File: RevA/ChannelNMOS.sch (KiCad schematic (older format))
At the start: 2 parts, among them U2 RAx4_4 1K

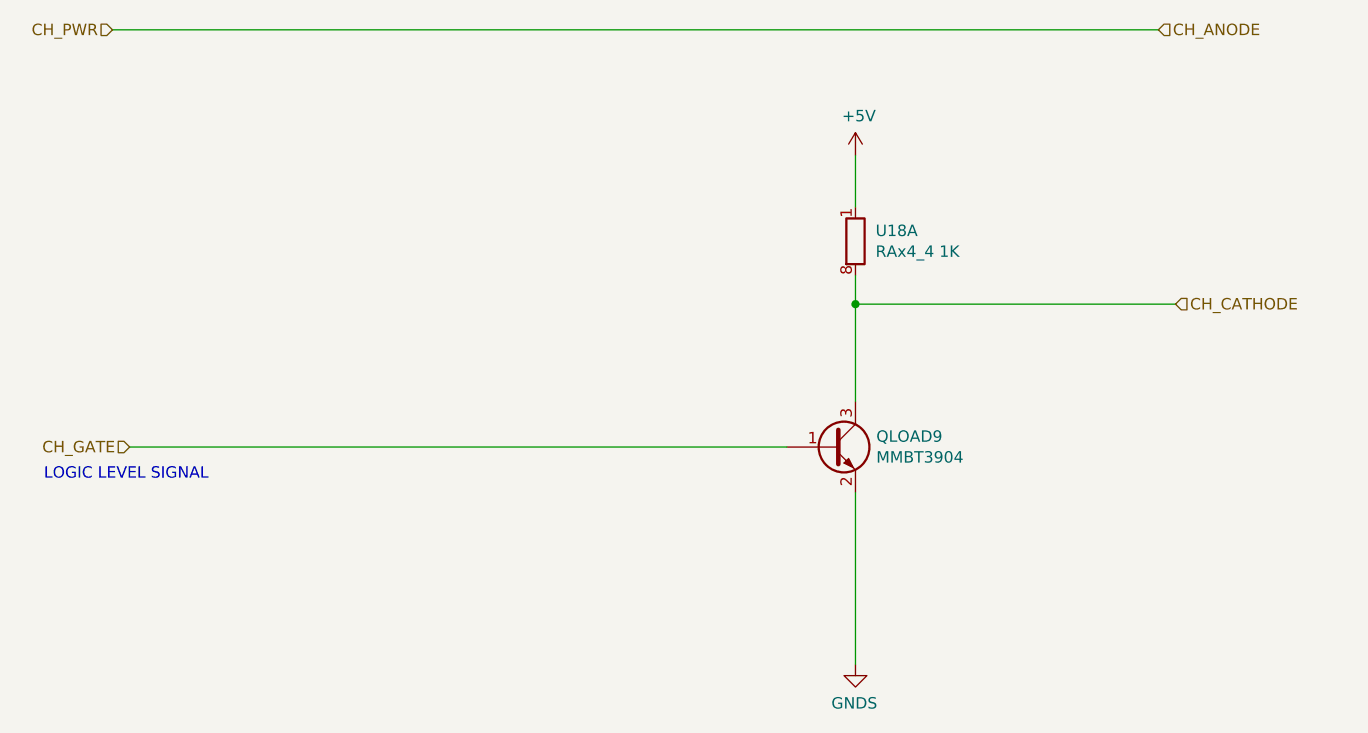
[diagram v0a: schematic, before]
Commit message: updated HW
changed single gang PTD901 to dual gang concentric PTH901
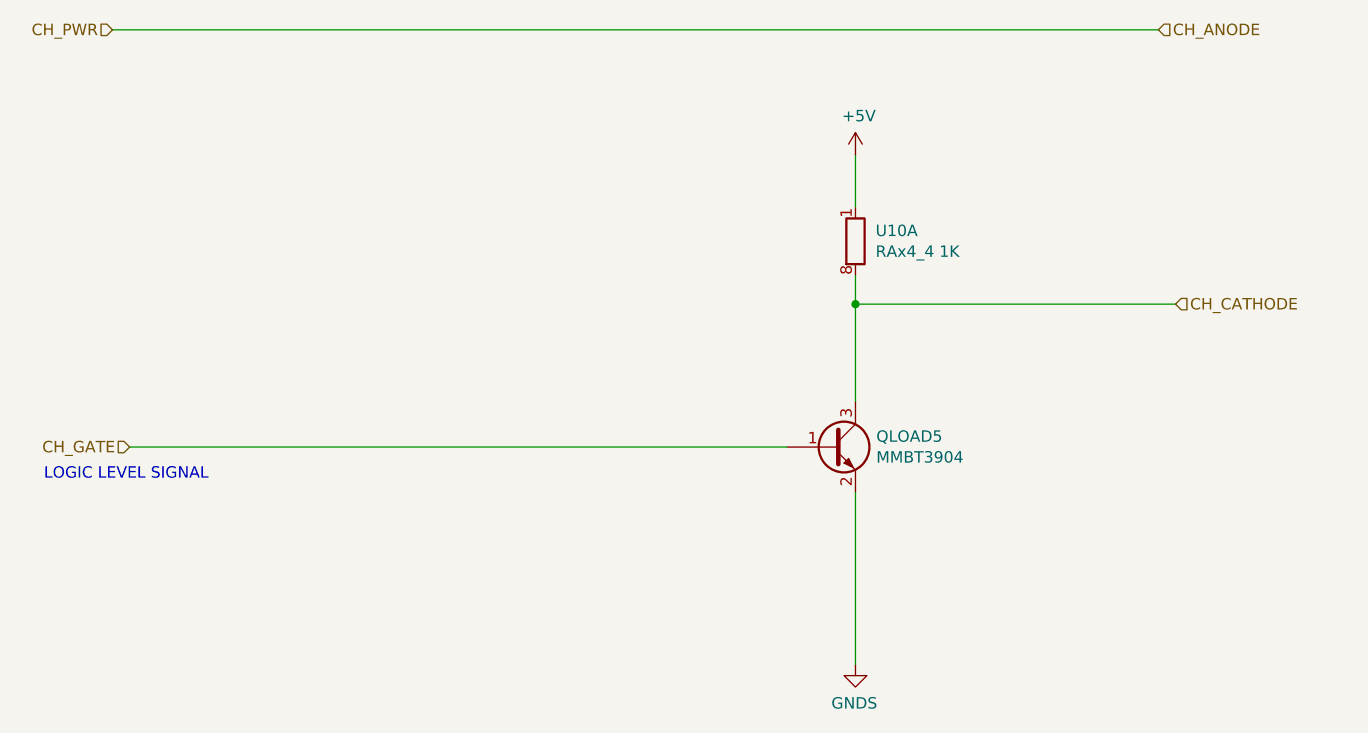
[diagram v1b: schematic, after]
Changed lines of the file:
@@
 AR Path="/5E2651B2/5E02AF0C" Ref="#PWR06"  Part="1"
 AR Path="/5E29F140/5E02AF0C" Ref="#PWR01"  Part="1"
-F 0 "#PWR01" H 6600 5575 50  0001 C CNN
+F 0 "#PWR068" H 6600 5575 50  0001 C CNN
 F 1 "GNDS" H 6605 5654 50  0000 C CNN
 F 2 "" H 6600 5825 50  0001 C CNN
@@
 AR Path="/5E2651B2/5E7FADEB" Ref="#PWR055"  Part="1"
 AR Path="/5E29F140/5E7FADEB" Ref="#PWR056"  Part="1"
-F 0 "#PWR056" H 6600 3450 50  0001 C CNN
+F 0 "#PWR057" H 6600 3450 50  0001 C CNN
 F 1 "+5V" H 6615 3773 50  0000 C CNN
 F 2 "" H 6600 3600 50  0001 C CNN
@@
 AR Path="/5E2651B2/5EAB52D0" Ref="U16"  Part="1"
 AR Path="/5E29F140/5EAB52D0" Ref="U18"  Part="1"
-F 0 "U18" V 6554 4063 50  0000 L CNN
+F 0 "U10" V 6554 4063 50  0000 L CNN
 F 1 "RAx4_4 1K" V 6645 4063 50  0000 L CNN
 F 2 "Resistor_SMD:R_Array_Convex_4x0603" H 6600 3875 50  0001 C CNN
@@
 AR Path="/5E2651B2/5E01FEAF" Ref="QLOAD8"  Part="1"
 AR Path="/5E29F140/5E01FEAF" Ref="QLOAD9"  Part="1"
-F 0 "QLOAD9" H 6691 4921 50  0000 L CNN
+F 0 "QLOAD5" H 6691 4921 50  0000 L CNN
 F 1 "MMBT3904" H 6691 4830 50  0000 L CNN
 F 2 "Package_TO_SOT_SMD:SOT-23" H 6700 4800 50  0001 L CIN

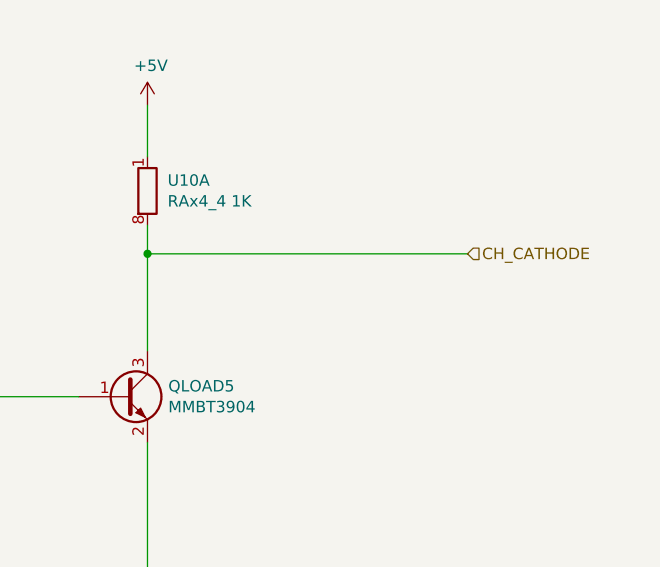
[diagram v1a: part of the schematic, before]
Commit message: Added some annotations to schematic
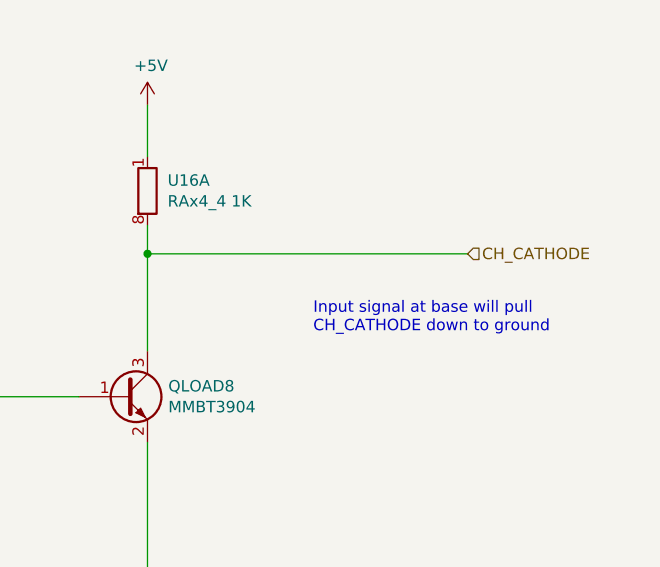
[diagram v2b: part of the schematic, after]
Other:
- note added: "Input signal at base will pull \nCH_CATHODE down to ground"
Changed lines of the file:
@@
 $Descr A4 11693 8268
 encoding utf-8
-Sheet 27 29
+Sheet 26 29
 Title ""
 Date ""
@@
 AR Path="/5E2651B2/5E02AF0C" Ref="#PWR06"  Part="1"
 AR Path="/5E29F140/5E02AF0C" Ref="#PWR01"  Part="1"
-F 0 "#PWR068" H 6600 5575 50  0001 C CNN
+F 0 "#PWR06" H 6600 5575 50  0001 C CNN
 F 1 "GNDS" H 6605 5654 50  0000 C CNN
 F 2 "" H 6600 5825 50  0001 C CNN
@@
 AR Path="/5E2651B2/5E7FADEB" Ref="#PWR055"  Part="1"
 AR Path="/5E29F140/5E7FADEB" Ref="#PWR056"  Part="1"
-F 0 "#PWR057" H 6600 3450 50  0001 C CNN
+F 0 "#PWR055" H 6600 3450 50  0001 C CNN
 F 1 "+5V" H 6615 3773 50  0000 C CNN
 F 2 "" H 6600 3600 50  0001 C CNN
@@
 AR Path="/5E2651B2/5EAB52D0" Ref="U16"  Part="1"
 AR Path="/5E29F140/5EAB52D0" Ref="U18"  Part="1"
-F 0 "U10" V 6554 4063 50  0000 L CNN
+F 0 "U16" V 6554 4063 50  0000 L CNN
 F 1 "RAx4_4 1K" V 6645 4063 50  0000 L CNN
 F 2 "Resistor_SMD:R_Array_Convex_4x0603" H 6600 3875 50  0001 C CNN
@@
 AR Path="/5E2651B2/5E01FEAF" Ref="QLOAD8"  Part="1"
 AR Path="/5E29F140/5E01FEAF" Ref="QLOAD9"  Part="1"
-F 0 "QLOAD5" H 6691 4921 50  0000 L CNN
+F 0 "QLOAD8" H 6691 4921 50  0000 L CNN
 F 1 "MMBT3904" H 6691 4830 50  0000 L CNN
 F 2 "Package_TO_SOT_SMD:SOT-23" H 6700 4800 50  0001 L CIN
@@
 	1    0    0    -1
 $EndComp
+Text Notes 7325 4600 0    50   ~ 0
+Input signal at base will pull \nCH_CATHODE down to ground
 $EndSCHEMATC
